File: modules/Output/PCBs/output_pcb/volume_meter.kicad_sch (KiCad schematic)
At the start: 35 parts, among them U10 TL074, U11 TL074

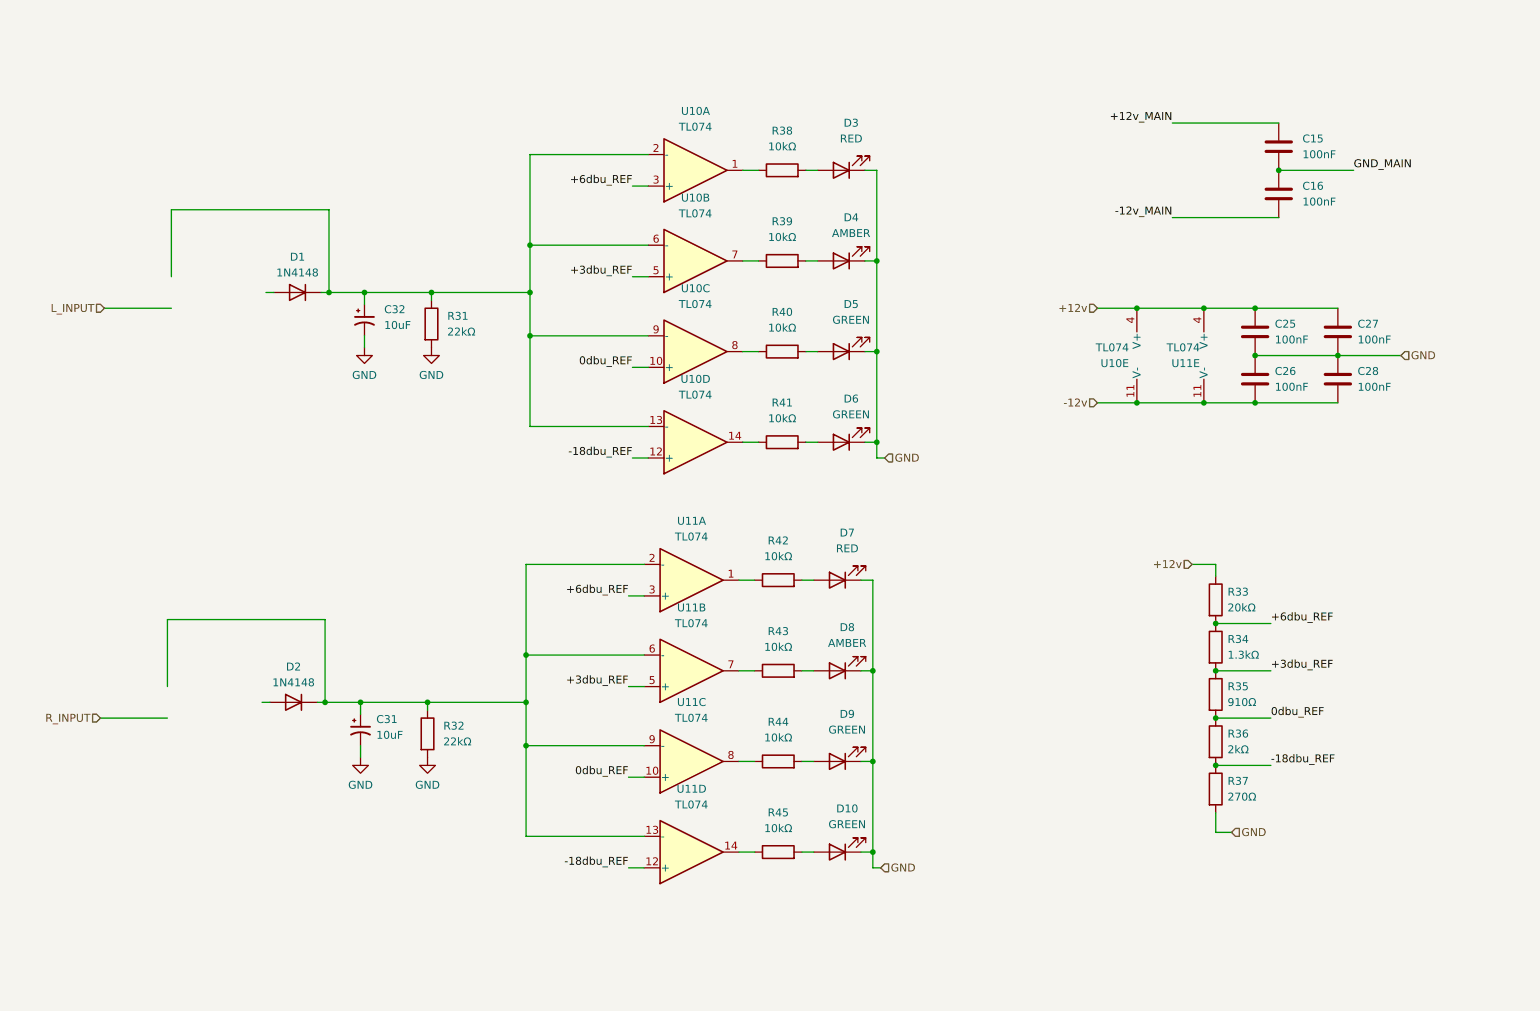
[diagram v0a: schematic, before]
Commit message: finish output PCB
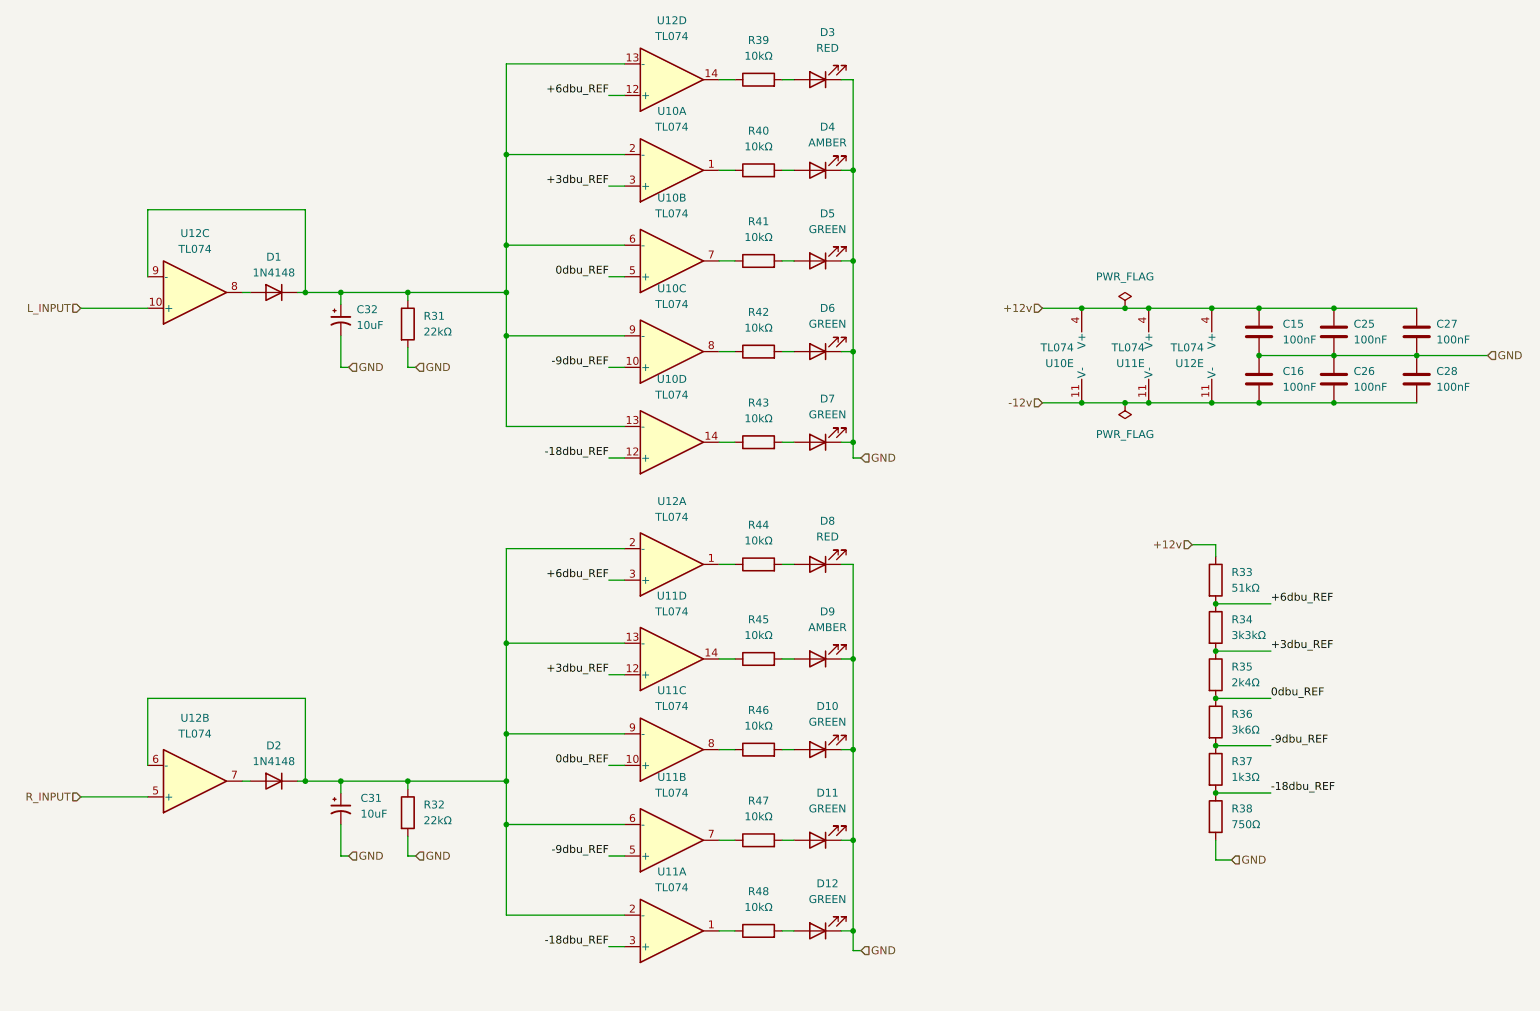
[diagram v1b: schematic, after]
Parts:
- added D12, D7: GREEN, LED_THT:LED_D3.0mm, symbol Device:LED
- added R46, R47, R48: 10kΩ, Resistor_THT:R_Axial_DIN0207_L6.3mm_D2.5mm_P10.16mm_Horizontal, symbol Device:R
- added U12: TL074, Package_DIP:DIP-14_W7.62mm, symbol Amplifier_Operational:TL074
- R33: value 20kΩ -> 51kΩ
- R34: value 1.3kΩ -> 3k3kΩ
- R35: value 910Ω -> 2k4Ω
- R36: value 2kΩ -> 3k6Ω
- R37: value 270Ω -> 1k3Ω
- R38: value 10kΩ -> 750Ω
- renumbered D9 to D10, D10 to D11, D7 to D8, D8 to D9
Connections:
- net +12v_MAIN is gone; now on net +12v: C15.1
- net -12v_MAIN is gone; now on net -12v: C16.2
- net GND_MAIN is gone; now on net GND: C15.2, C16.1
- net +12v: now also U12.4 (V+)
- net +3dbu_REF: now also U10.3 (+), U11.12 (+); no longer U10.5 (+), U11.5 (+)
- net +6dbu_REF: now also U12.12 (+), U12.3 (+); no longer U10.3 (+), U11.3 (+)
- net -12v: now also U12.11 (V-)
- net -18dbu_REF: now also R37.2, R38.1, U11.3 (+); no longer R36.2, R37.1, U11.12 (+)
- net 0dbu_REF: now also U10.5 (+); no longer U10.10 (+)
- net GND: now also R38.2, D12.1 (K), D7.1 (K); no longer R37.2
- net L_INPUT: now also U12.10 (+)
- net R_INPUT: now also U12.5 (+)
- net at R45.2: now also D9.2 (A); no longer D11.2 (A)
- net at U10.1: now also R40.1; no longer R38.1
- net at D3.2 (A): now also R39.2; no longer R38.2
- net at U10.8: now also R42.1; no longer R40.1
- net at R40.2: now also D4.2 (A); no longer D5.2 (A)
- net at R41.1: now also U10.7; no longer U10.14
- net at R41.2: now also D5.2 (A); no longer D6.2 (A)
- net at C31.1, D2.1 (K), R32.1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: now also U12.2 (-), U12.6 (-)
- net at R44.1: now also U12.1; no longer U11.8
- net at R44.2: now also D8.2 (A); no longer D10.2 (A)
- net at C32.1, D1.1 (K), R31.1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: now also U12.13 (-), U12.9 (-)
- net at R39.1: now also U12.14; no longer U10.7
- net at U11.1: now also R48.1; no longer R42.1
- net at R42.2: now also D6.2 (A); no longer D8.2 (A)
- net at U11.7: now also R47.1; no longer R43.1
- net at D1.2 (A): now also U12.8
- net at R43.2: now also D7.2 (A); no longer D9.2 (A)
- net at D2.2 (A): now also U12.7
- new net: R46.1, U11.8
- new net: D10.2 (A), R46.2
- new net: D11.2 (A), R47.2
- new net: D12.2 (A), R48.2
- new net: R43.1, U10.14
- new net -9dbu_REF: R36.2, R37.1, U10.10 (+), U11.5 (+)
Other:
- moved on the sheet: C15, C16, C25, C26, C27, C28, C31, C32, D1, D10, D11, D2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

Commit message: fix polarity mismatch bugs in output pcb
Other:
- company: (none) -> Free Modular
- title: (none) -> Output

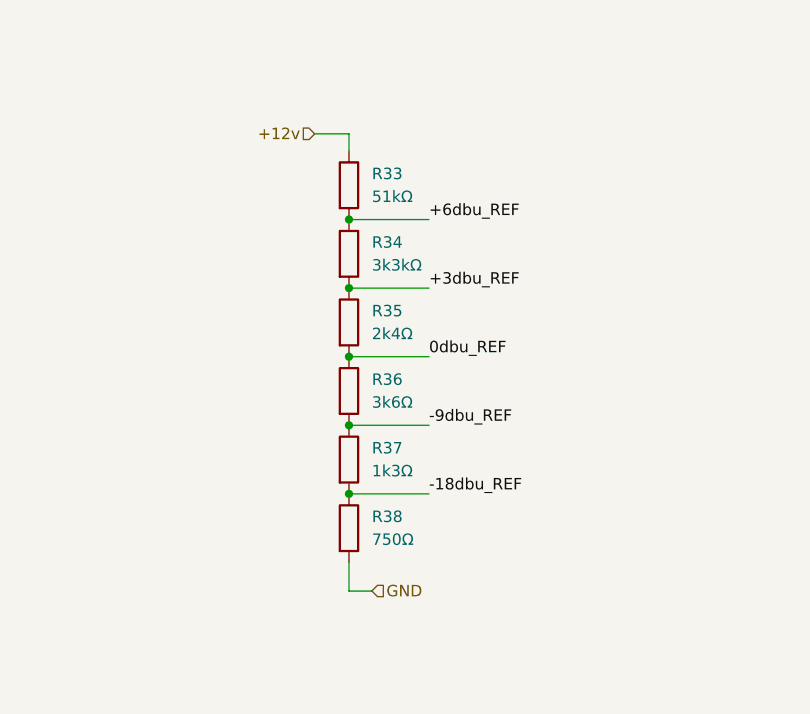
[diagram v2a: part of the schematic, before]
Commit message: adjusted resistor values in output
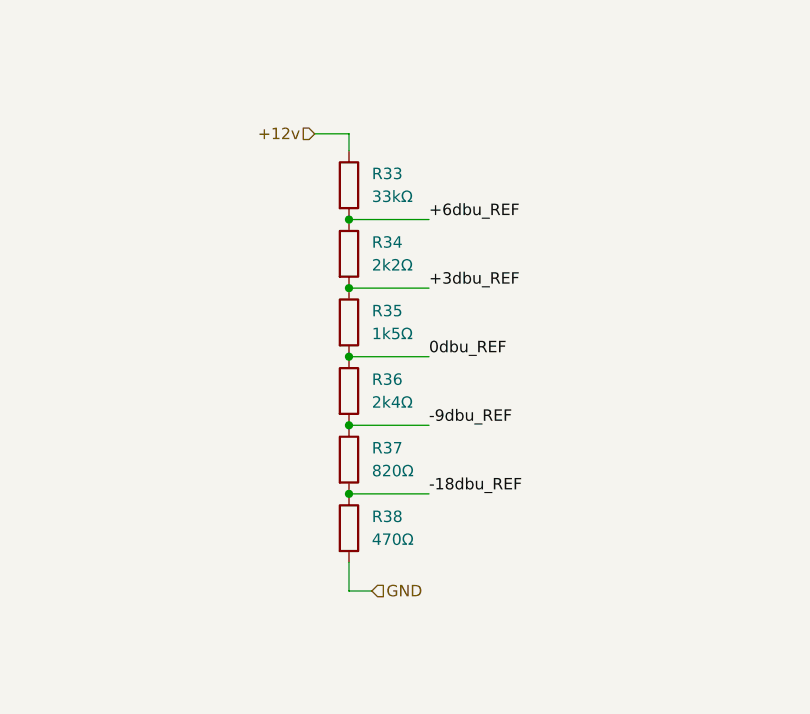
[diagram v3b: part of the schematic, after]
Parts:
- R33: value 51kΩ -> 33kΩ
- R34: value 3k3kΩ -> 2k2Ω
- R35: value 2k4Ω -> 1k5Ω
- R36: value 3k6Ω -> 2k4Ω
- R37: value 1k3Ω -> 820Ω
- R38: value 750Ω -> 470Ω
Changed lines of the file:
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@@
 		(fields_autoplaced yes)
 		(property "Reference" "R36"
-			(at 218.44 128.905 0)
-			(effects
-				(font
-					(size 1.27 1.27)
-				)
-				(justify left)
-			)
-		)
-		(property "Value" "3k6Ω"
-			(at 218.44 131.445 0)
+			(at 218.44 128.9049 0)
+			(effects
+				(font
+					(size 1.27 1.27)
+				)
+				(justify left)
+			)
+		)
+		(property "Value" "2k4Ω"
+			(at 218.44 131.4449 0)
 			(effects
 				(font
@@
 		(fields_autoplaced yes)
 		(property "Reference" "R33"
-			(at 218.44 106.045 0)
-			(effects
-				(font
-					(size 1.27 1.27)
-				)
-				(justify left)
-			)
-		)
-		(property "Value" "51kΩ"
-			(at 218.44 108.585 0)
+			(at 218.44 106.0449 0)
+			(effects
+				(font
+					(size 1.27 1.27)
+				)
+				(justify left)
+			)
+		)
+		(property "Value" "33kΩ"
+			(at 218.44 108.5849 0)
 			(effects
 				(font
@@
 		(fields_autoplaced yes)
 		(property "Reference" "R38"
-			(at 218.44 144.145 0)
-			(effects
-				(font
-					(size 1.27 1.27)
-				)
-				(justify left)
-			)
-		)
-		(property "Value" "750Ω"
-			(at 218.44 146.685 0)
+			(at 218.44 144.1449 0)
+			(effects
+				(font
+					(size 1.27 1.27)
+				)
+				(justify left)
+			)
+		)
+		(property "Value" "470Ω"
+			(at 218.44 146.6849 0)
 			(effects
 				(font
@@
 		(fields_autoplaced yes)
 		(property "Reference" "R37"
-			(at 218.44 136.525 0)
-			(effects
-				(font
-					(size 1.27 1.27)
-				)
-				(justify left)
-			)
-		)
-		(property "Value" "1k3Ω"
-			(at 218.44 139.065 0)
+			(at 218.44 136.5249 0)
+			(effects
+				(font
+					(size 1.27 1.27)
+				)
+				(justify left)
+			)
+		)
+		(property "Value" "820Ω"
+			(at 218.44 139.0649 0)
 			(effects
 				(font
@@
 		(fields_autoplaced yes)
 		(property "Reference" "R34"
-			(at 218.44 113.665 0)
-			(effects
-				(font
-					(size 1.27 1.27)
-				)
-				(justify left)
-			)
-		)
-		(property "Value" "3k3kΩ"
-			(at 218.44 116.205 0)
+			(at 218.44 113.6649 0)
+			(effects
+				(font
+					(size 1.27 1.27)
+				)
+				(justify left)
+			)
+		)
+		(property "Value" "2k2Ω"
+			(at 218.44 116.2049 0)
 			(effects
 				(font
@@
 		(fields_autoplaced yes)
 		(property "Reference" "R35"
-			(at 218.44 121.285 0)
-			(effects
-				(font
-					(size 1.27 1.27)
-				)
-				(justify left)
-			)
-		)
-		(property "Value" "2k4Ω"
-			(at 218.44 123.825 0)
-			(effects
-				(font
+			(at 218.44 121.2849 0)
+			(effects
+				(font
+					(size 1.27 1.27)
+				)
+				(justify left)
+			)
+		)
+		(property "Value" "1k5Ω"
+			(at 218.44 123.8249 0)
+			(effects
+				(font
